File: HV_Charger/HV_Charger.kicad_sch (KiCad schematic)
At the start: 25 parts

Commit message: Updated
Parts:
- removed D?: D_Schottky, symbol Device:D_Schottky
- removed F?: 5A, symbol Device:Fuse
- removed J?: Relay, symbol Connector_Generic:Conn_01x02
- removed TP? (x2): 12V, TestPoint:TestPoint_Pad_4.0x4.0mm, symbol Connector:TestPoint
- added J?: Expansion_Port, symbol Connector_Generic:Conn_01x04
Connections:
- net 24V: now also J?.1 (Pin_1)
- net AMS -: no longer J?.2 (Pin_2), R?.2
- net CAN H: now also J?.3 (Pin_3)
- net CAN L: now also J?.4 (Pin_4)
- net GND: now also J?.2 (Pin_2)
- net IMD -: no longer J?.2 (Pin_2), R?.2
- new net AMS: J?.2 (Pin_2), R?.2
- new net IMD: J?.2 (Pin_2), R?.2
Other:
- added sheet 12v-24v Booster (boost.kicad_sch)
- note added: "IMD & AMS LEDs"
- note added: "Shutdown Path"
- moved on the sheet: D?, J?, JP?, R?

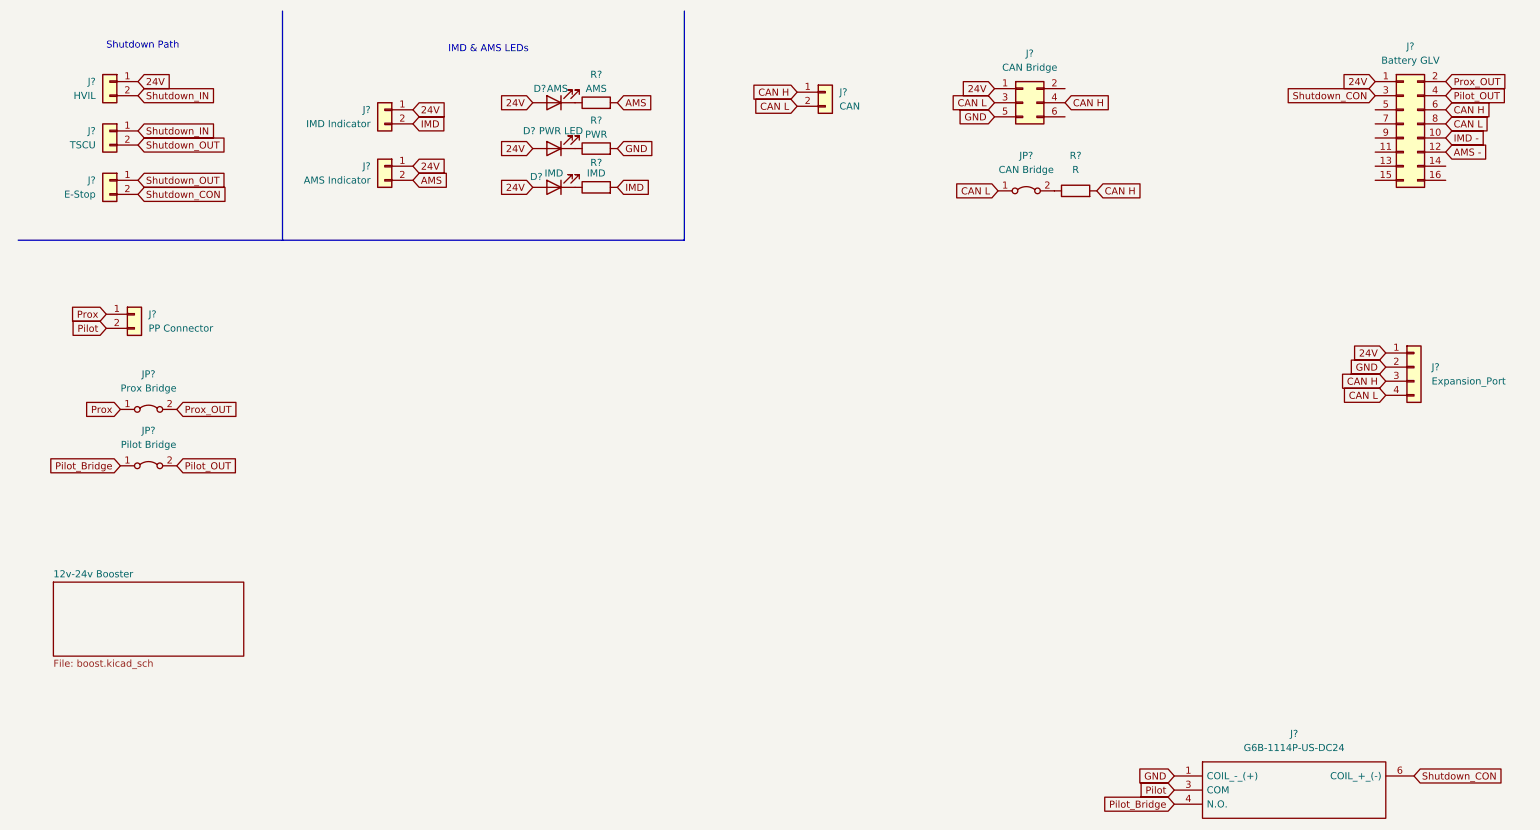
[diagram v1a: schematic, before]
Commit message: Fixed Rylan issues, pls switch diodes on pmos
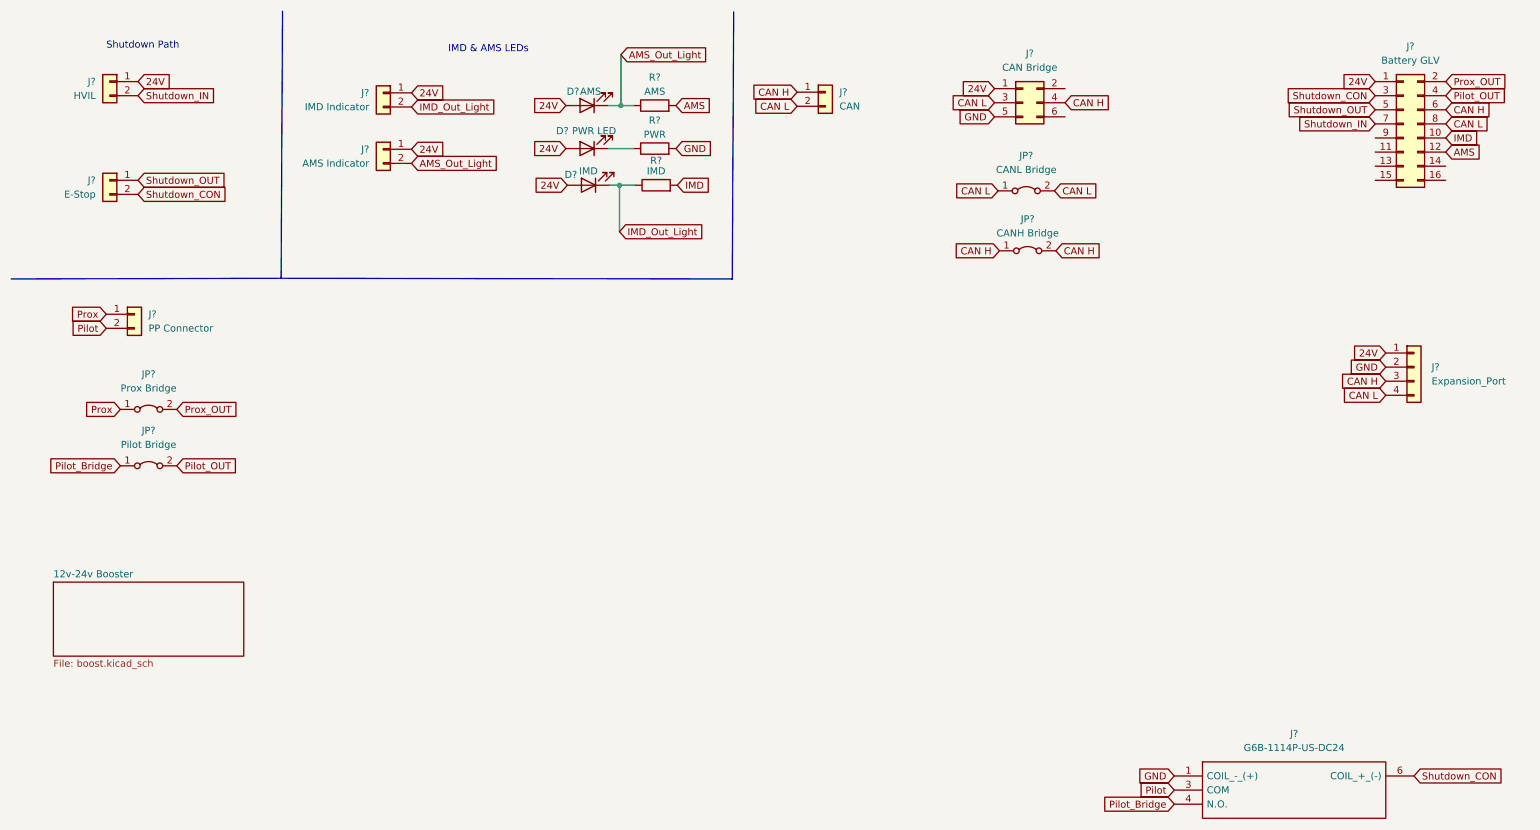
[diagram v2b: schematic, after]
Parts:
- removed J?: TSCU, symbol Connector_Generic:Conn_01x02
- removed R?: R, symbol Device:R
- added JP?: CANH Bridge, symbol Jumper:Jumper_2_Bridged
- JP?: value CAN Bridge -> CANL Bridge
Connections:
- net AMS - is gone; now on net AMS: J?.12 (Pin_12)
- net IMD - is gone; now on net IMD: J?.10 (Pin_10)
- net AMS: no longer J?.2 (Pin_2)
- net CAN H: now also JP?.1 (A), JP?.2 (B)
- net CAN L: now also JP?.2 (B)
- net IMD: no longer J?.2 (Pin_2)
- net Shutdown_IN: now also J?.7 (Pin_7)
- net Shutdown_OUT: now also J?.5 (Pin_5)
- net IMD_Out_Light: now reaches D?.1 (K), R?.1
- net IMD_Out_Light: now also J?.2 (Pin_2)
- net AMS_Out_Light: now reaches D?.1 (K), R?.1
- net AMS_Out_Light: now also J?.2 (Pin_2)
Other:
- moved on the sheet: D?, J?, R?
